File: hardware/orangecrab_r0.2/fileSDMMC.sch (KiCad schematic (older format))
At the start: 6 parts, among them J4 MicroSd

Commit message: hw: Update microSD card
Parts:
- J4: footprint gkl_conn:micro_sd_1051620001 -> gkl_conn:molex_microsd_1040310811
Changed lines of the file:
@@
 F 0 "J4" H 5700 4450 50  0000 L CNN
 F 1 "MicroSd" H 5650 4350 50  0000 L CNN
-F 2 "gkl_conn:micro_sd_1051620001" H 5650 3750 50  0001 C CNN
+F 2 "gkl_conn:molex_microsd_1040310811" H 5650 3750 50  0001 C CNN
 F 3 "~" H 5650 3750 50  0001 C CNN
 F 4 "1051620001" H 5650 3750 50  0001 C CNN "PN"

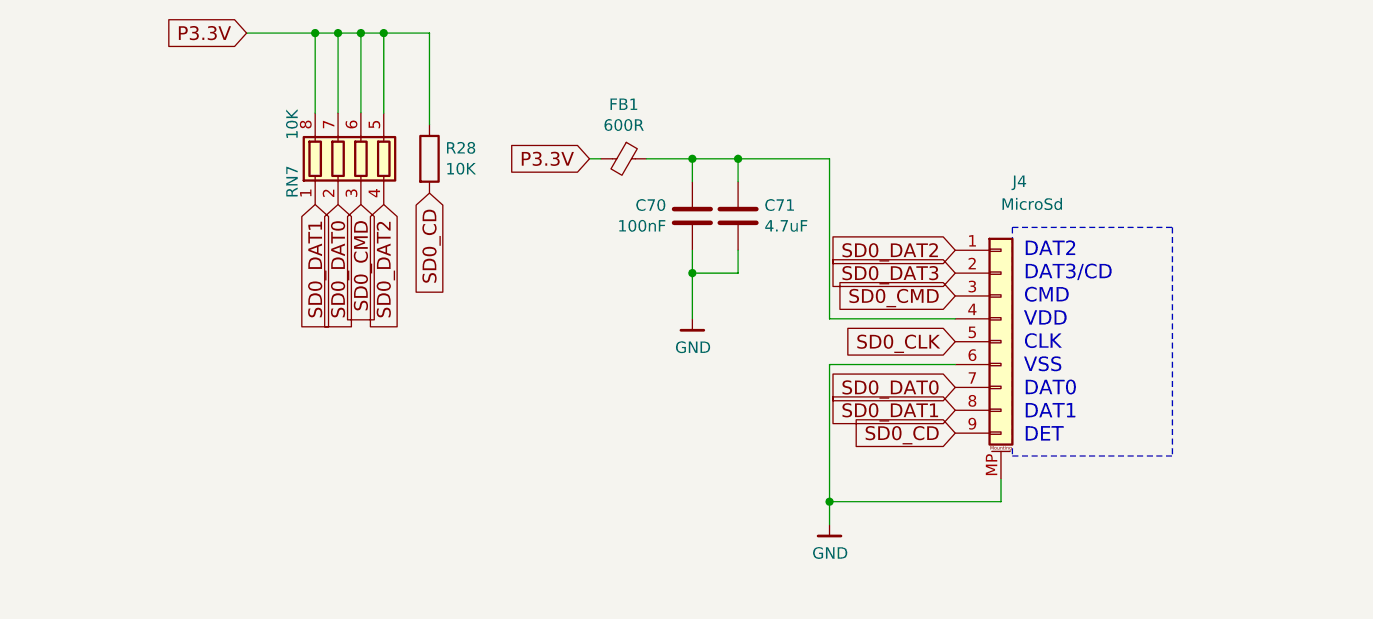
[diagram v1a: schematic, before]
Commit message: hw: Update board with 3d models Finish pin-swaps and routing of open changes General cleanups
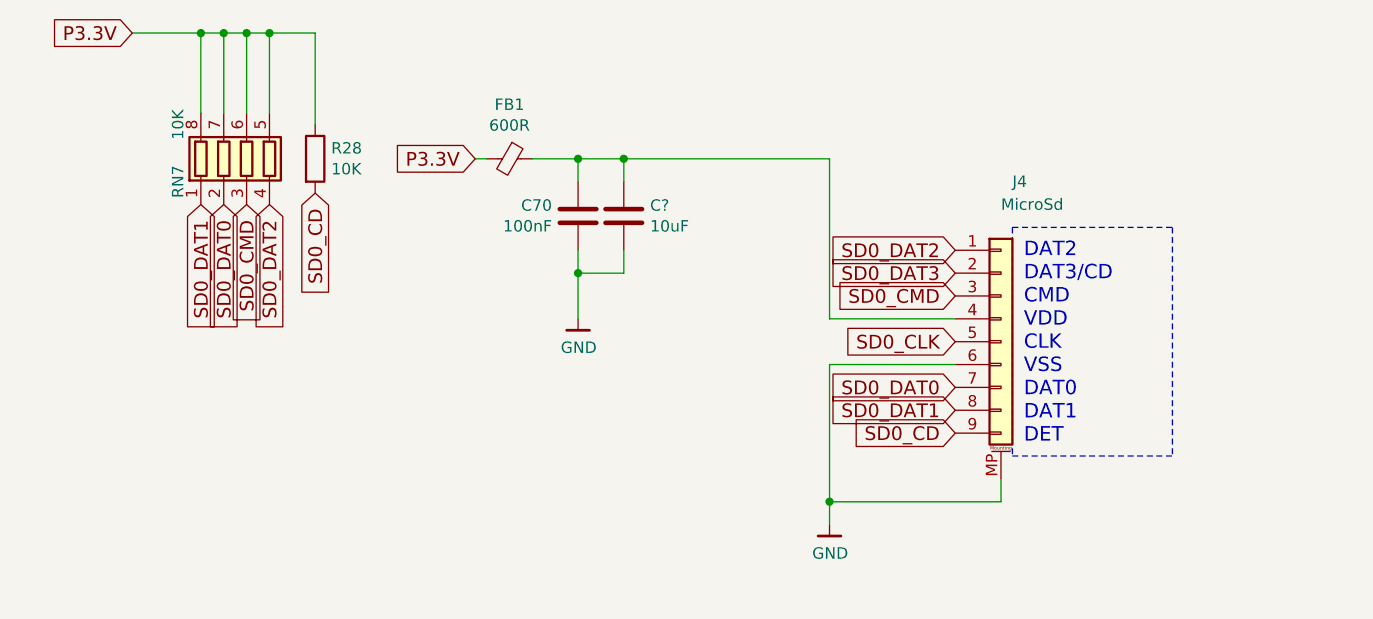
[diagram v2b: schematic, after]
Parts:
- removed C71: 4.7uF, Capacitor_SMD:C_0603_1608Metric, symbol Device:C
- added C?: 10uF, Capacitor_SMD:C_0402_1005Metric, symbol Device:C
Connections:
- net GND: now also C?.1
- net at C70.2, FB1.1, J4.4 (Pin_4): now also C?.2
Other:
- moved on the sheet: C70, FB1, R28, RN7
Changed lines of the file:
@@
 Wire Notes Line
 	5700 3250 6400 3250
-Text GLabel 3850 2950 0    60   Input ~ 0
+Text GLabel 3350 2950 0    60   Input ~ 0
 P3.3V
 $Comp
 L Device:Ferrite_Bead_Small FB1
 U 1 1 5D5BE84B
-P 4000 2950
-F 0 "FB1" V 3763 2950 50  0000 C CNN
-F 1 "600R" V 3854 2950 50  0000 C CNN
-F 2 "Inductor_SMD:L_0402_1005Metric" V 3930 2950 50  0001 C CNN
-F 3 "~" H 4000 2950 50  0001 C CNN
-F 4 "Murata Electronics North America" H 4000 2950 50  0001 C CNN "Mfg"
-F 5 "BLM15AG601SN1D" H 4000 2950 50  0001 C CNN "PN"
-	1    4000 2950
+P 3500 2950
+F 0 "FB1" V 3263 2950 50  0000 C CNN
+F 1 "600R" V 3354 2950 50  0000 C CNN
+F 2 "Inductor_SMD:L_0402_1005Metric" V 3430 2950 50  0001 C CNN
+F 3 "~" H 3500 2950 50  0001 C CNN
+F 4 "Murata Electronics North America" H 3500 2950 50  0001 C CNN "Mfg"
+F 5 "BLM15AG601SN1D" H 3500 2950 50  0001 C CNN "PN"
+	1    3500 2950
 	0    1    1    0
-$EndComp
-$Comp
-L Device:C C71
-U 1 1 5D5BF142
-P 4500 3200
-F 0 "C71" H 4615 3246 50  0000 L CNN
-F 1 "4.7uF" H 4615 3155 50  0000 L CNN
-F 2 "Capacitor_SMD:C_0603_1608Metric" H 4538 3050 50  0001 C CNN
-F 3 "~" H 4500 3200 50  0001 C CNN
-F 4 "Samsung Electro-Mechanics" H 4500 3200 50  0001 C CNN "Mfg"
-F 5 "CL10A475KP8NNNC" H 4500 3200 50  0001 C CNN "PN"
-	1    4500 3200
-	1    0    0    -1
 $EndComp
 $Comp
 L Device:C C70
 U 1 1 5D5BF444
-P 4300 3200
-F 0 "C70" H 4186 3154 50  0000 R CNN
-F 1 "100nF" H 4186 3245 50  0000 R CNN
-F 2 "Capacitor_SMD:C_0201_0603Metric" H 4338 3050 50  0001 C CNN
-F 3 "~" H 4300 3200 50  0001 C CNN
-F 4 "Samsung Electro-Mechanics" H 4300 3200 50  0001 C CNN "Mfg"
-F 5 "CL03A104KQ3NNNC" H 4300 3200 50  0001 C CNN "PN"
-	1    4300 3200
+P 3800 3200
+F 0 "C70" H 3686 3154 50  0000 R CNN
+F 1 "100nF" H 3686 3245 50  0000 R CNN
+F 2 "Capacitor_SMD:C_0201_0603Metric" H 3838 3050 50  0001 C CNN
+F 3 "~" H 3800 3200 50  0001 C CNN
+F 4 "Samsung Electro-Mechanics" H 3800 3200 50  0001 C CNN "Mfg"
+F 5 "CL03A104KQ3NNNC" H 3800 3200 50  0001 C CNN "PN"
+	1    3800 3200
 	1    0    0    1
 $EndComp
 Wire Wire Line
-	4100 2950 4300 2950
+	3600 2950 3800 2950
 Wire Wire Line
 	4900 2950 4900 3650
 Wire Wire Line
-	4500 3050 4500 2950
-Connection ~ 4500 2950
+	4000 3050 4000 2950
+Connection ~ 4000 2950
 Wire Wire Line
-	4500 2950 4900 2950
+	4000 2950 4900 2950
 Wire Wire Line
-	4300 3050 4300 2950
-Connection ~ 4300 2950
+	3800 3050 3800 2950
+Connection ~ 3800 2950
 Wire Wire Line
-	4300 2950 4500 2950
+	3800 2950 4000 2950
 Wire Wire Line
-	3900 2950 3850 2950
+	3400 2950 3350 2950
 Wire Wire Line
-	4300 3350 4300 3450
+	3800 3350 3800 3450
 Wire Wire Line
-	4500 3350 4500 3450
+	4000 3350 4000 3450
 Wire Wire Line
-	4500 3450 4300 3450
-Connection ~ 4300 3450
+	4000 3450 3800 3450
+Connection ~ 3800 3450
 Wire Wire Line
-	4300 3450 4300 3650
+	3800 3450 3800 3650
 $Comp
 L gkl_power:GND #PWR0159
 U 1 1 5D5C1FC1
-P 4300 3650
-F 0 "#PWR0159" H 4300 3400 50  0001 C CNN
-F 1 "GND" H 4303 3524 50  0000 C CNN
-F 2 "" H 4200 3300 50  0001 C CNN
-F 3 "" H 4300 3650 50  0001 C CNN
-	1    4300 3650
+P 3800 3650
+F 0 "#PWR0159" H 3800 3400 50  0001 C CNN
+F 1 "GND" H 3803 3524 50  0000 C CNN
+F 2 "" H 3700 3300 50  0001 C CNN
+F 3 "" H 3800 3650 50  0001 C CNN
+	1    3800 3650
 	1    0    0    -1
 $EndComp
@@
 L Device:R_Pack04 RN?
 U 1 1 5D5ABE41
-P 2850 2950
+P 2350 2950
 AR Path="/5ABD38F2/5D5ABE41" Ref="RN?"  Part="1"
 AR Path="/5AC0A2A0/5D5ABE41" Ref="RN7"  Part="1"
-F 0 "RN7" V 2550 2850 50  0000 C CNN
-F 1 "10K" V 2550 3100 50  0000 C CNN
-F 2 "Resistor_SMD:R_Array_Convex_4x0402" V 3125 2950 50  0001 C CNN
-F 3 "~" H 2850 2950 50  0001 C CNN
-F 4 "RAVF104DJT10K0" H 2850 2950 50  0001 C CNN "PN"
-F 5 "Stackpole Electronics Inc" H 2850 2950 50  0001 C CNN "Mfg"
-	1    2850 2950
+F 0 "RN7" V 2050 2850 50  0000 C CNN
+F 1 "10K" V 2050 3100 50  0000 C CNN
+F 2 "Resistor_SMD:R_Array_Convex_4x0402" V 2625 2950 50  0001 C CNN
+F 3 "~" H 2350 2950 50  0001 C CNN
+F 4 "RAVF104DJT10K0" H 2350 2950 50  0001 C CNN "PN"
+F 5 "Stackpole Electronics Inc" H 2350 2950 50  0001 C CNN "Mfg"
+	1    2350 2950
 	1    0    0    -1
 $EndComp
-Text GLabel 2350 2400 0    60   Input ~ 0
+Text GLabel 1850 2400 0    60   Input ~ 0
 P3.3V
 Wire Wire Line
-	2350 2400 2650 2400
+	1850 2400 2150 2400
 Wire Wire Line
-	2650 2400 2650 2750
+	2150 2400 2150 2750
 Wire Wire Line
-	2650 2400 2750 2400
+	2150 2400 2250 2400
 Wire Wire Line
-	2750 2400 2750 2750
-Connection ~ 2650 2400
+	2250 2400 2250 2750
+Connection ~ 2150 2400
 Wire Wire Line
-	2750 2400 2850 2400
+	2250 2400 2350 2400
 Wire Wire Line
-	2850 2400 2850 2750
-Connection ~ 2750 2400
+	2350 2400 2350 2750
+Connection ~ 2250 2400
 Wire Wire Line
-	2850 2400 2950 2400
+	2350 2400 2450 2400
 Wire Wire Line
-	2950 2400 2950 2750
-Connection ~ 2850 2400
-Text GLabel 2950 3150 3    60   Input ~ 0
+	2450 2400 2450 2750
+Connection ~ 2350 2400
+Text GLabel 2450 3150 3    60   Input ~ 0
 SD0_DAT2
-Text GLabel 2850 3150 3    60   Input ~ 0
+Text GLabel 2350 3150 3    60   Input ~ 0
 SD0_CMD
-Text GLabel 2750 3150 3    60   Input ~ 0
+Text GLabel 2250 3150 3    60   Input ~ 0
 SD0_DAT0
-Text GLabel 2650 3150 3    60   Input ~ 0
+Text GLabel 2150 3150 3    60   Input ~ 0
 SD0_DAT1
 $Comp
 L Device:R R28
 U 1 1 5D5AD51E
-P 3150 2950
-F 0 "R28" H 3220 2996 50  0000 L CNN
-F 1 "10K" H 3220 2905 50  0000 L CNN
-F 2 "Resistor_SMD:R_0201_0603Metric" V 3080 2950 50  0001 C CNN
-F 3 "~" H 3150 2950 50  0001 C CNN
-F 4 "‎Yageo‎" H 3150 2950 50  0001 C CNN "Mfg"
-F 5 "RC0201FR-0710KL" H 3150 2950 50  0001 C CNN "PN"
-	1    3150 2950
+P 2650 2950
+F 0 "R28" H 2720 2996 50  0000 L CNN
+F 1 "10K" H 2720 2905 50  0000 L CNN
+F 2 "Resistor_SMD:R_0201_0603Metric" V 2580 2950 50  0001 C CNN
+F 3 "~" H 2650 2950 50  0001 C CNN
+F 4 "‎Yageo‎" H 2650 2950 50  0001 C CNN "Mfg"
+F 5 "RC0201FR-0710KL" H 2650 2950 50  0001 C CNN "PN"
+	1    2650 2950
 	1    0    0    -1
 $EndComp
-Text GLabel 3150 3100 3    60   Input ~ 0
+Text GLabel 2650 3100 3    60   Input ~ 0
 SD0_CD
 Wire Wire Line
-	2950 2400 3150 2400
+	2450 2400 2650 2400
 Wire Wire Line
-	3150 2400 3150 2800
-Connection ~ 2950 2400
+	2650 2400 2650 2800
+Connection ~ 2450 2400
+$Comp
+L Device:C C?
+U 1 1 5E89F19A
+P 4000 3200
+AR Path="/5D1738DB/5E89F19A" Ref="C?"  Part="1"
+AR Path="/5AC0A2A0/5E89F19A" Ref="C?"  Part="1"
+F 0 "C?" H 3885 3154 50  0000 R CNN
+F 1 "10uF" H 3885 3245 50  0000 R CNN
+F 2 "Capacitor_SMD:C_0402_1005Metric" H 4038 3050 50  0001 C CNN
+F 3 "~" H 4000 3200 50  0001 C CNN
+F 4 "Murata Electronics North America" H 4000 3200 50  0001 C CNN "Mfg"
+F 5 "GRM155R60J106ME15D" H 4000 3200 50  0001 C CNN "PN"
+	1    4000 3200
+	-1   0    0    1
+$EndComp
 $EndSCHEMATC

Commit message: hw: Route last FPGA I/O to A[0-5]
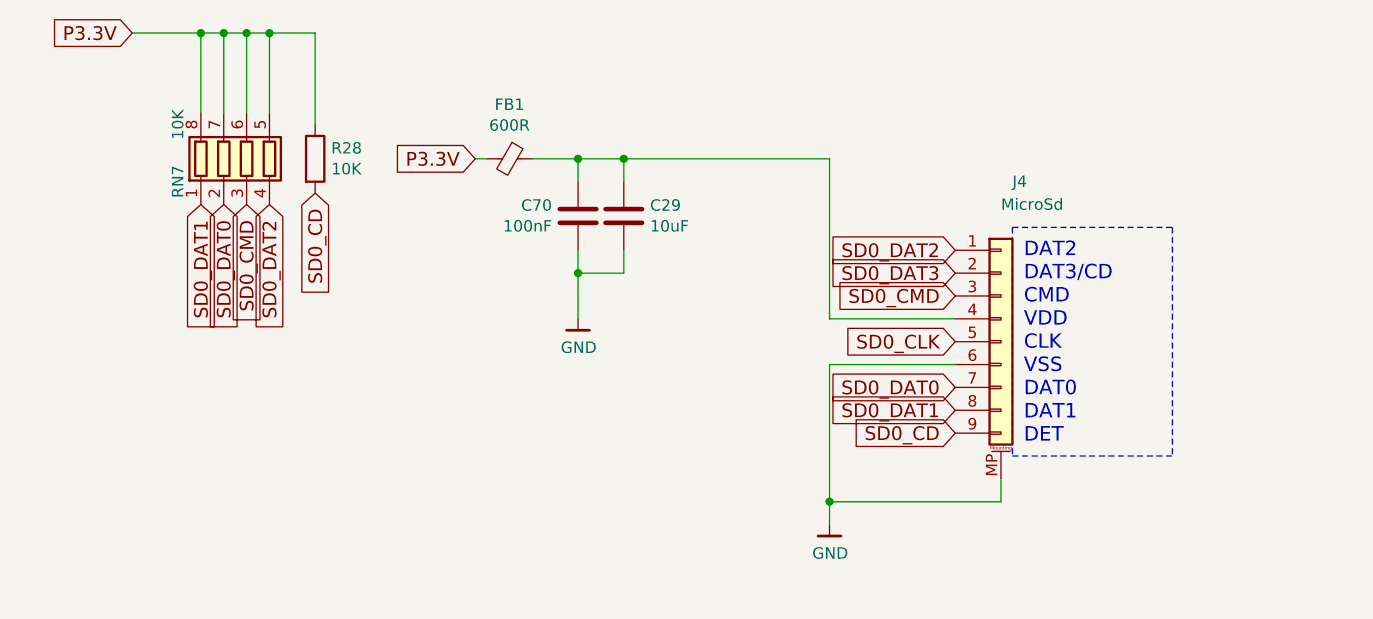
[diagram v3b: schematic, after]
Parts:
- gave numbers to parts that had none: 1
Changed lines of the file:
@@
 P 4000 3200
 AR Path="/5D1738DB/5E89F19A" Ref="C?"  Part="1"
-AR Path="/5AC0A2A0/5E89F19A" Ref="C?"  Part="1"
-F 0 "C?" H 3885 3154 50  0000 R CNN
+AR Path="/5AC0A2A0/5E89F19A" Ref="C29"  Part="1"
+F 0 "C29" H 3885 3154 50  0000 R CNN
 F 1 "10uF" H 3885 3245 50  0000 R CNN
 F 2 "Capacitor_SMD:C_0402_1005Metric" H 4038 3050 50  0001 C CNN

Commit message: hardware/orangecrab_r0.2: r0.2 Release
Prepared KiCad files for release
Create production folder
Add pdf schematic
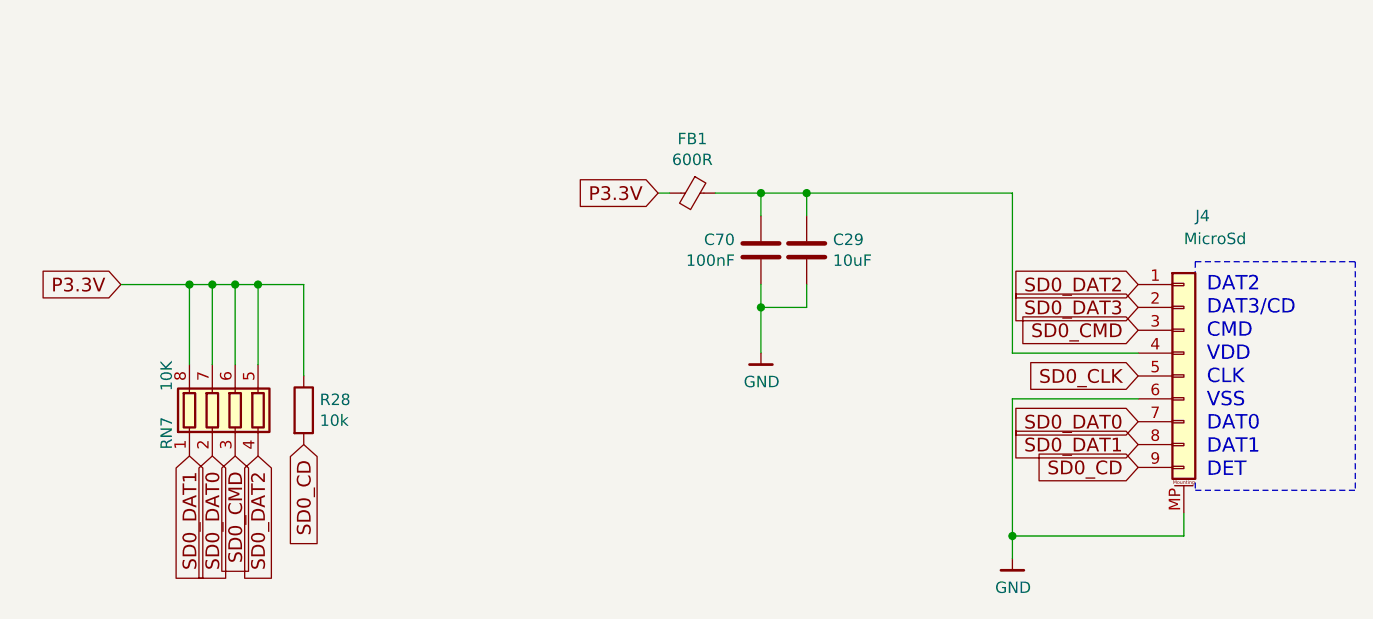
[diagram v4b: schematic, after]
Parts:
- J4: PN 1051620001 -> 1040310811
- R28: value 10K -> 10k
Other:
- moved on the sheet: C29, C70, FB1, J4, R28, RN7
